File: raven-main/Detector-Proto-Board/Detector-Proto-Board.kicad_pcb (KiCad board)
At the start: 2 copper layers, 26.3 x 26.5 mm, 22 parts, among them IC1 ADA4817-1ARDZ-R7, J1 Conn_01x04, U9 TLV3201AIDCKT

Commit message: Add 2.5V pedestal bias to fix TIA operating point on single supply
Fix amplifier DC operating point with 2.5V pedestal bias

The ADA4817 TIA output rested at 0V with +IN grounded, but on a single
0-5V supply the output cannot swing below ~1.4V, pinning the amplifier
against the rail. Bias +IN to a 2.5V pedestal so the output rests
mid-range and photocurrent pulses swing into its linear region.

- Add pedestal divider: R33/R34 (10k) + C40 (1uF) generating Vped (2.5V)
- Reroute IC1 +IN from GND to Vped
- Re-reference threshold divider to Vped: R28 to GND, R32 to Vped
- R31 200K->300K, R32 200->300 to keep the 5-25mV hysteresis band
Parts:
- added C40: 1uF, Capacitor_SMD:C_0402_1005Metric, F.Cu at (131.8, 84.5)
- added R33: 10k, Resistor_SMD:R_0402_1005Metric, F.Cu at (129.0, 84.5)
- added R34: 10k, Resistor_SMD:R_0402_1005Metric, F.Cu at (129.0, 86.5)
- R31: value 200K -> 300K
- R32: value 200 -> 300
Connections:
- IC1 pad 3: GND -> /Vped
- R28 pad 2: +5V -> GND
- R32 pad 1: GND -> /Vped

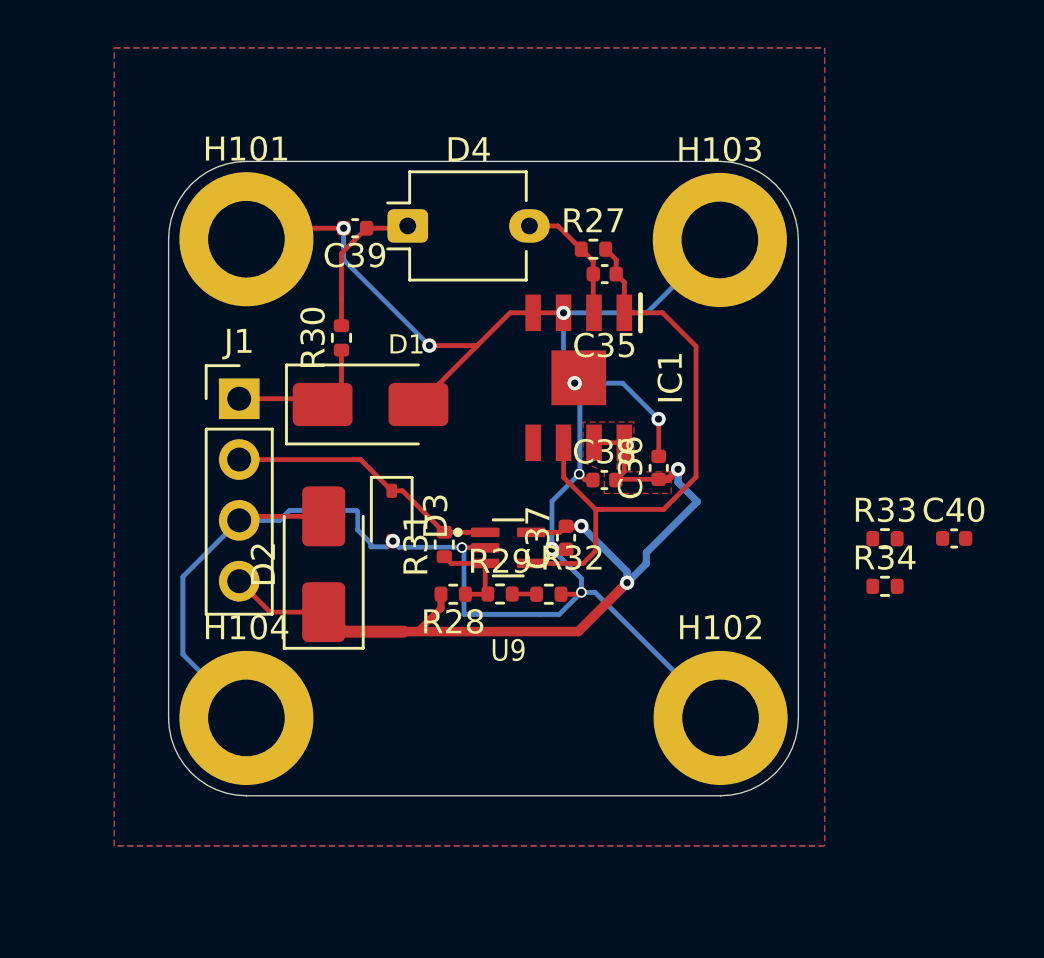
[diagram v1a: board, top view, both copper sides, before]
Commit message: Route Vped, enlarge board, fix shorts from net changes
Correct pedestal to 2.0 V — 2.5 V exceeded the ADA4817's input
common-mode ceiling (+Vs - 2.7 V). Revised divider keeps the original
10-50 mV threshold and 5-25 mV hysteresis spec.

- R33 15k/R34 10k -> Vped = 2.00 V; R31 390K, R32 390R, R29 2k trimmer
- Place R33/R34/C40 between the bottom mounting pads; route /Vped
  (F.Cu bus + B.Cu trunk, 3 vias) and +5V feed
- Remove stale copper left by the net changes (shorts, clearance,
  hole clearance, mask bridges)
- Grow board to 31.8 x 32.0 mm, corner radius 6 mm, mounting hole
  pattern unchanged
- All vias 0.6/0.3; drop dangling +5V stub; H103 back on grid
- Drop 0402 silk body bars

TODO: refdes placement unfinished — text was set to 0.7 mm, below the
0.8 mm board minimum. Needs resizing to 0.8 mm and re-placing to clear
pads and neighbouring silk.
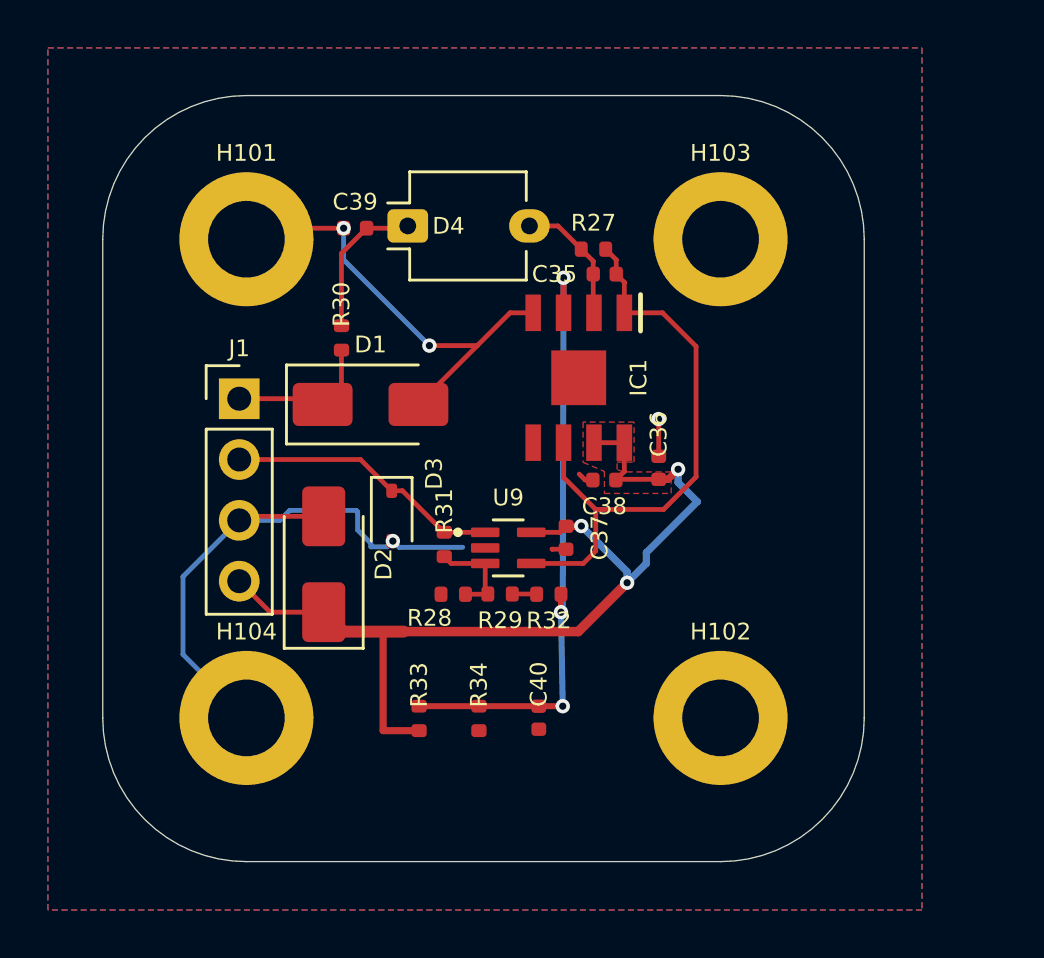
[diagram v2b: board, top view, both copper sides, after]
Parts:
- moved R33 20.9 mm to (109.5, 92.0), turned to 90 degrees
- moved C40 18.9 mm to (114.5, 92.0), turned to -90 degrees
- moved R34 17.8 mm to (112.0, 92.0), turned to -90 degrees
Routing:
- net GND: track 91.7 -> 47.1 mm, vias 10 -> 4
- net /Vped: track 0.00 -> 26.2 mm, vias 0 -> 3
- net +5V: track 37.9 -> 41.0 mm
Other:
- board size 26.3 x 26.5 mm -> 31.8 x 32 mm
